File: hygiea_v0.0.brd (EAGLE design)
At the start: 38 x 61.8 mm, 45 parts, among them U1 3.3V/150mA, U2 BNO055, U3 CRYSTAL_8X3.8SMD

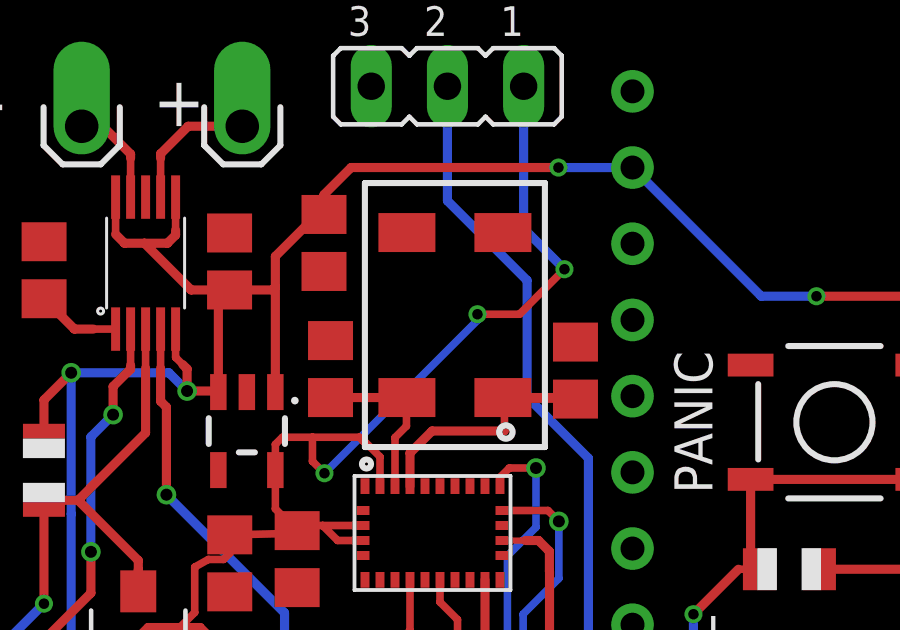
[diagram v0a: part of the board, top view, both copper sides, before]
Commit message: Se movió la resistencia del crystal del BNO055
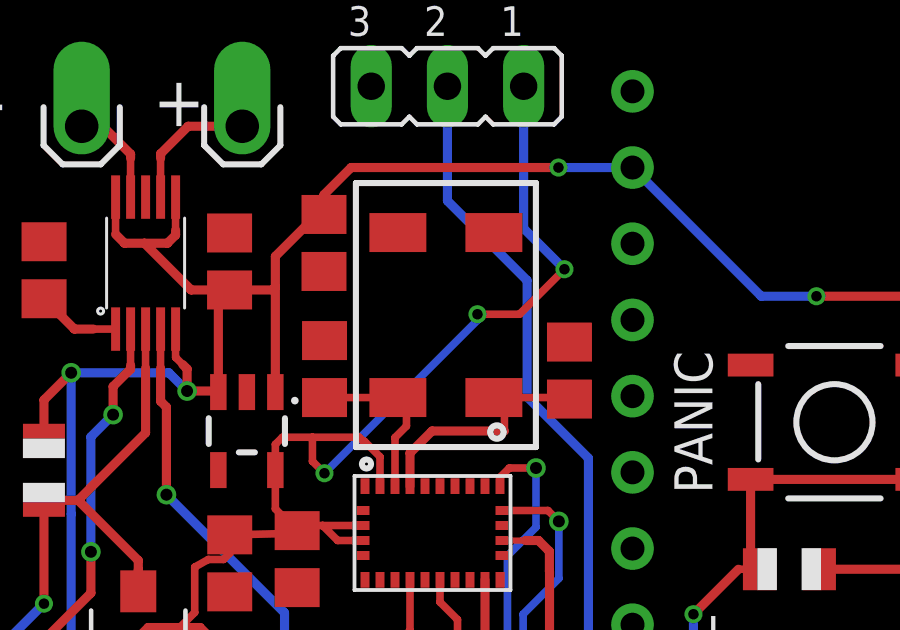
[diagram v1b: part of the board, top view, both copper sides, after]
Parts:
- moved U3 0.30 mm to (19.3, 51.1)
- moved C7 0.20 mm to (15.3, 49.3)
- moved C8 0.20 mm to (23.5, 49.2)
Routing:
- net XIN_A: track 8.20 -> 5.96 mm
- net XOUT_A: track 10.5 -> 8.80 mm
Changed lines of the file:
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@@
 <attribute name="VALUE" x="19.835" y="37.479" size="1.27" layer="27" rot="R90"/>
 </element>
-<element name="C7" library="rcl" library_urn="urn:adsk.eagle:library:334" package="C0805" package3d_urn="urn:adsk.eagle:package:23617/2" value="22pF" x="15.503" y="49.272" smashed="yes" rot="R90">
-<attribute name="SPICEPREFIX" value="C" x="15.503" y="49.272" size="1.778" layer="27" rot="R90" display="off"/>
-<attribute name="VALUE" x="18.043" y="48.002" size="1.27" layer="27" rot="R90"/>
-</element>
-<element name="C8" library="rcl" library_urn="urn:adsk.eagle:library:334" package="C0805" package3d_urn="urn:adsk.eagle:package:23617/2" value="22pF" x="23.668" y="49.222" smashed="yes" rot="R90">
-<attribute name="SPICEPREFIX" value="C" x="23.668" y="49.222" size="1.778" layer="27" rot="R90" display="off"/>
-<attribute name="VALUE" x="26.208" y="47.952" size="1.27" layer="27" rot="R90"/>
+<element name="C7" library="rcl" library_urn="urn:adsk.eagle:library:334" package="C0805" package3d_urn="urn:adsk.eagle:package:23617/2" value="22pF" x="15.303" y="49.272" smashed="yes" rot="R90">
+<attribute name="SPICEPREFIX" value="C" x="15.303" y="49.272" size="1.778" layer="27" rot="R90" display="off"/>
+<attribute name="VALUE" x="17.843" y="48.002" size="1.27" layer="27" rot="R90"/>
+</element>
+<element name="C8" library="rcl" library_urn="urn:adsk.eagle:library:334" package="C0805" package3d_urn="urn:adsk.eagle:package:23617/2" value="22pF" x="23.468" y="49.222" smashed="yes" rot="R90">
+<attribute name="SPICEPREFIX" value="C" x="23.468" y="49.222" size="1.778" layer="27" rot="R90" display="off"/>
+<attribute name="VALUE" x="26.008" y="47.952" size="1.27" layer="27" rot="R90"/>
 </element>
 <element name="C9" library="rcl" library_urn="urn:adsk.eagle:library:334" package="C0805" package3d_urn="urn:adsk.eagle:package:23617/2" value="0.1uF" x="8.16" y="28.442" smashed="yes" rot="R270">
@@
 <attribute name="VALUE" x="16.19803125" y="40.503140625" size="1.27186875" layer="27"/>
 </element>
-<element name="U3" library="hygiea_parts" package="PM8.0X3.8MM" value="CRYSTAL_8X3.8SMD" x="19.649" y="51.073" smashed="yes" rot="R90">
-<attribute name="VALUE" x="18.649" y="49.773" size="0.6096" layer="27" rot="R90"/>
+<element name="U3" library="hygiea_parts" package="PM8.0X3.8MM" value="CRYSTAL_8X3.8SMD" x="19.349" y="51.073" smashed="yes" rot="R90">
+<attribute name="VALUE" x="18.349" y="49.773" size="0.6096" layer="27" rot="R90"/>
 </element>
 <element name="ALT_SENSOR" library="hygiea_parts" package="LGA8" value="MPL3115A2" x="13.079" y="28.774" smashed="yes">
@@
 <contactref element="C7" pad="1"/>
 <contactref element="U3" pad="4"/>
-<wire x1="18.049" y1="48.323" x2="18.034" y2="48.323" width="0.254" layer="1"/>
-<wire x1="18.034" y1="48.323" x2="15.504" y2="48.323" width="0.254" layer="1"/>
+<wire x1="17.749" y1="48.323" x2="18.034" y2="48.323" width="0.254" layer="1"/>
 <wire x1="17.652" y1="45.3705" x2="17.652" y2="46.989" width="0.254" layer="1"/>
-<wire x1="17.652" y1="46.989" x2="18.034" y2="47.371" width="0.254" layer="1"/>
-<wire x1="18.034" y1="47.371" x2="18.034" y2="48.323" width="0.254" layer="1"/>
-<wire x1="18.049" y1="48.323" x2="15.504" y2="48.323" width="0.3048" layer="1"/>
-<wire x1="15.504" y1="48.323" x2="15.503" y2="48.322" width="0.3048" layer="1"/>
+<wire x1="18.034" y1="47.371" x2="17.652" y2="46.989" width="0.254" layer="1"/>
+<wire x1="15.303" y1="48.322" x2="17.748" y2="48.322" width="0.254" layer="1"/>
+<wire x1="17.748" y1="48.322" x2="17.749" y2="48.323" width="0.254" layer="1"/>
+<wire x1="17.749" y1="48.323" x2="18.034" y2="48.038" width="0.254" layer="1"/>
+<wire x1="18.034" y1="48.038" x2="18.034" y2="47.371" width="0.254" layer="1"/>
 </signal>
 <signal name="XOUT_A">
@@
 <contactref element="C8" pad="1"/>
 <contactref element="U3" pad="1"/>
-<wire x1="23.668" y1="48.272" x2="21.3" y2="48.272" width="0.254" layer="1"/>
-<wire x1="21.3" y1="48.272" x2="21.249" y2="48.323" width="0.254" layer="1"/>
+<wire x1="21.3" y1="48.272" x2="20.949" y2="48.323" width="0.254" layer="1"/>
 <wire x1="21.3" y1="48.272" x2="21.3" y2="47.208" width="0.254" layer="1"/>
 <wire x1="18.152" y1="46.473" x2="18.152" y2="45.3705" width="0.3048" layer="1"/>
 <wire x1="21.3" y1="47.208" x2="18.887" y2="47.208" width="0.3048" layer="1"/>
 <wire x1="18.887" y1="47.208" x2="18.152" y2="46.473" width="0.3048" layer="1"/>
-<wire x1="21.249" y1="48.323" x2="23.617" y2="48.323" width="0.3048" layer="1"/>
-<wire x1="23.617" y1="48.323" x2="23.668" y2="48.272" width="0.3048" layer="1"/>
+<wire x1="23.617" y1="48.323" x2="23.468" y2="48.272" width="0.3048" layer="1"/>
+<wire x1="20.949" y1="48.323" x2="23.617" y2="48.323" width="0.254" layer="1"/>
 </signal>
 <signal name="IN/TRIG">

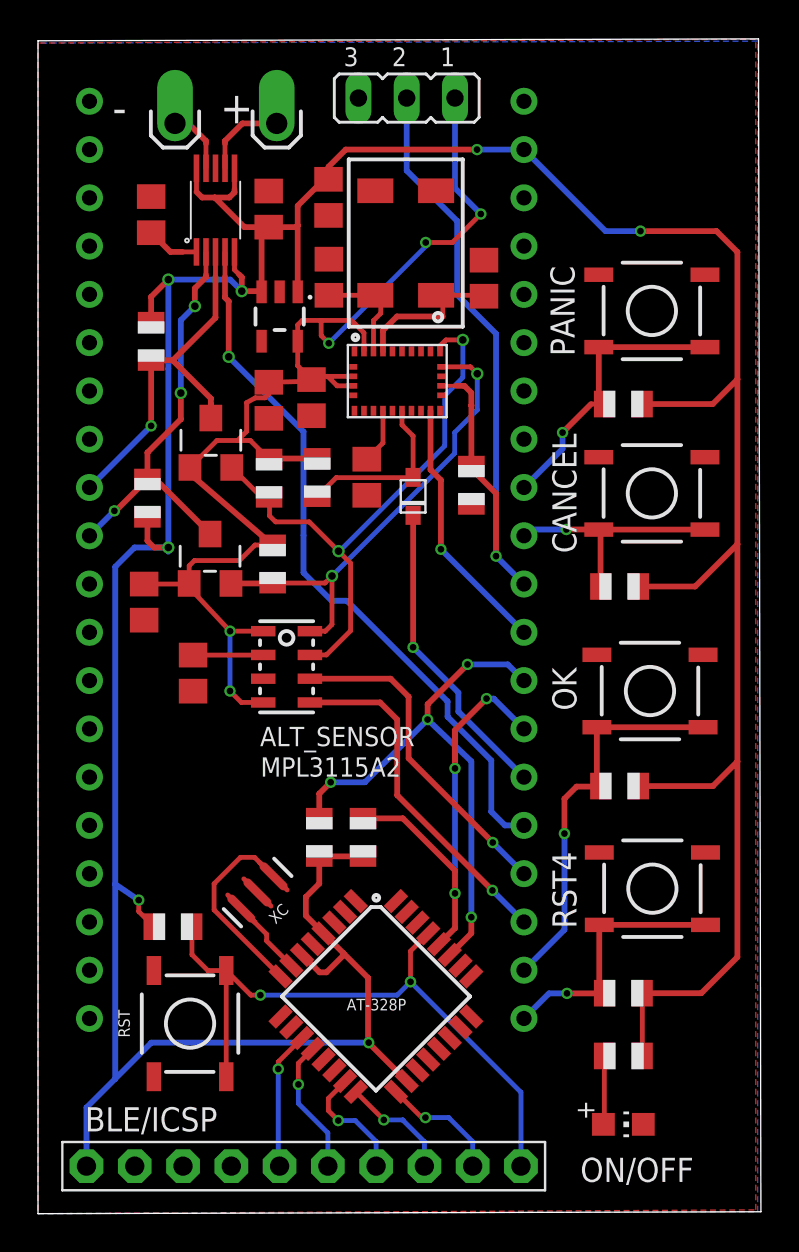
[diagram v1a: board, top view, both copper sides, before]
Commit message: Version barata, push buttons standar
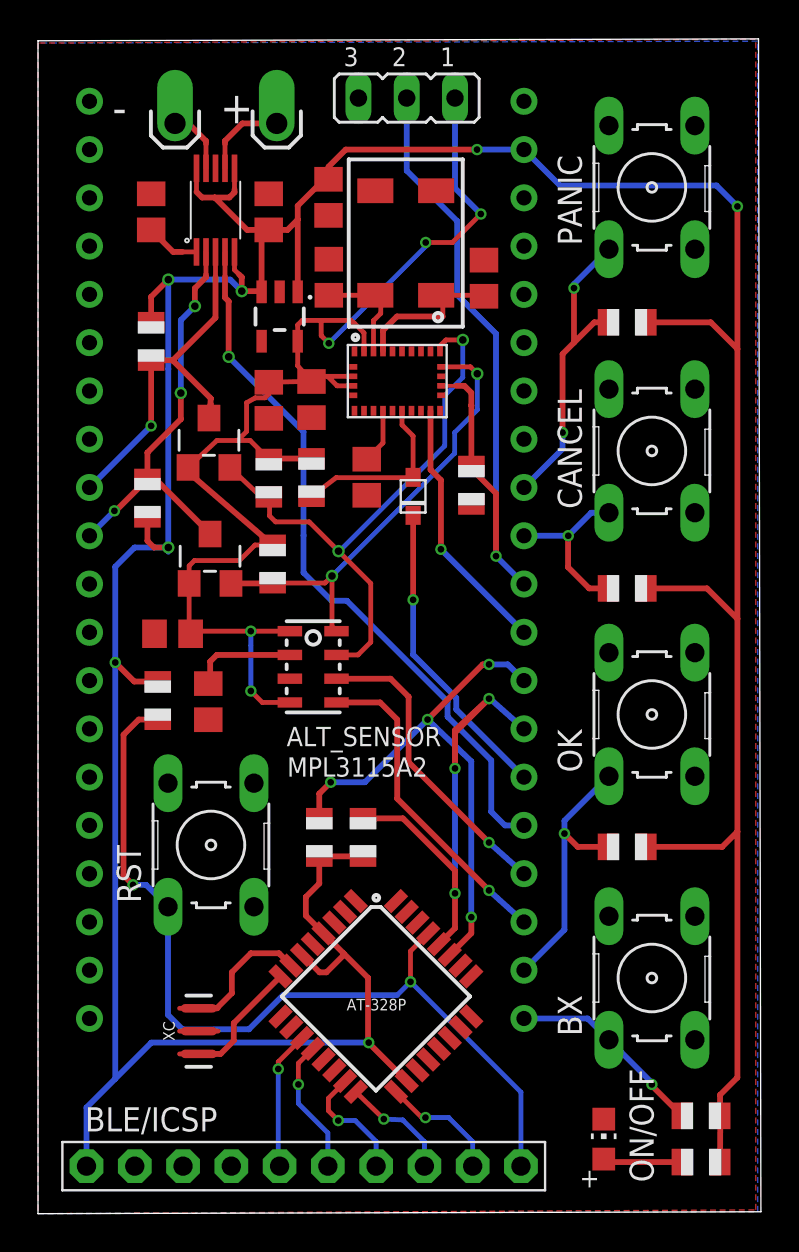
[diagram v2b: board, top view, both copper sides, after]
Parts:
- removed RST4: (no value), SparkFun-Switches:TACTILE_SWITCH_SMD_5.2MM
- added BX: (no value), switch-omron:B3F-10XX
- CANCEL, OK, PANIC, RST: device SparkFun-Switches:TACTILE_SWITCH_SMD_5.2MM -> switch-omron:B3F-10XX
- R10, R11, R12, R13: value (none) -> 1k
- R14: value (none) -> 330
- moved R7 11.9 mm to (6.30, 27.0), turned to 90 degrees
- moved RST 9.46 mm to (9.10, 19.4)
- moved XC 7.92 mm to (8.46, 9.61), turned to 90 degrees
- moved R13 7.64 mm to (34.9, 5.15)
- moved R14 6.92 mm to (34.9, 2.71)
- moved PANIC 6.50 mm to (32.3, 54.0), turned to 90 degrees
- moved R10 4.30 mm to (31.0, 46.9)
- moved R12 3.22 mm to (31.0, 19.3)
- moved C10 2.24 mm to (7.08, 30.5), turned to 180 degrees
- moved CANCEL 2.23 mm to (32.3, 40.1), turned to 90 degrees
- moved C9 1.70 mm to (8.96, 26.9)
- moved ALT_SENSOR 1.40 mm to (14.5, 28.8)
- moved ON/OFF 1.29 mm to (29.8, 3.92), turned to 0 degrees
- moved OK 1.24 mm to (32.3, 26.3), turned to 90 degrees
- moved R11 0.41 mm to (31.0, 32.9)
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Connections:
- net AT_RESET: now also RST.1; no longer RST.3, RST.4
- net B1: now also PANIC.1; no longer PANIC.3, PANIC.4
- net B2: now also CANCEL.1; no longer CANCEL.3, CANCEL.4
- net B3: now also OK.1; no longer OK.3, OK.4
- net B4: now also BX.1; no longer RST4.3, RST4.4
- net GND: now also BX.3, CANCEL.3, OK.3, PANIC.3, RST.3; no longer CANCEL.1, CANCEL.2, OK.1, OK.2, PANIC.1, PANIC.2, RST.1, RST.2, RST4.1, RST4.2
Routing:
- net AT_RESET: track 34.8 -> 47.4 mm
- net B3: track 20.8 -> 14.6 mm
- net XTAL_B: track 10.4 -> 6.53 mm
- net B2: track 12.9 -> 9.21 mm
- net B4: track 14.1 -> 10.5 mm
- net XTAL_A: track 4.09 -> 6.98 mm
- net SCL(2)_5V: track 25.7 -> 28.1 mm
- net N$2: track 3.69 -> 5.54 mm
- net 5V: track 208.9 -> 210.6 mm
- net B1: track 15.3 -> 16.6 mm, vias 1 -> 2
- net INT2: track 18.4 -> 17.0 mm
- net INT1: track 17.4 -> 16.1 mm
- net 3.3V: track 69.5 -> 70.4 mm
- net SCL_3V: track 25.2 -> 24.3 mm
- net N$1: track 3.62 -> 4.19 mm
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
